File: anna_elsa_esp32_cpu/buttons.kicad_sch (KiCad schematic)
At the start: 26 parts, among them J14 DOOR_SW, J22 BTN_SWITCHES, J23 BTN_LAMPS, Q3 ULN2803ADWR, U8 MCP23017-E_SO

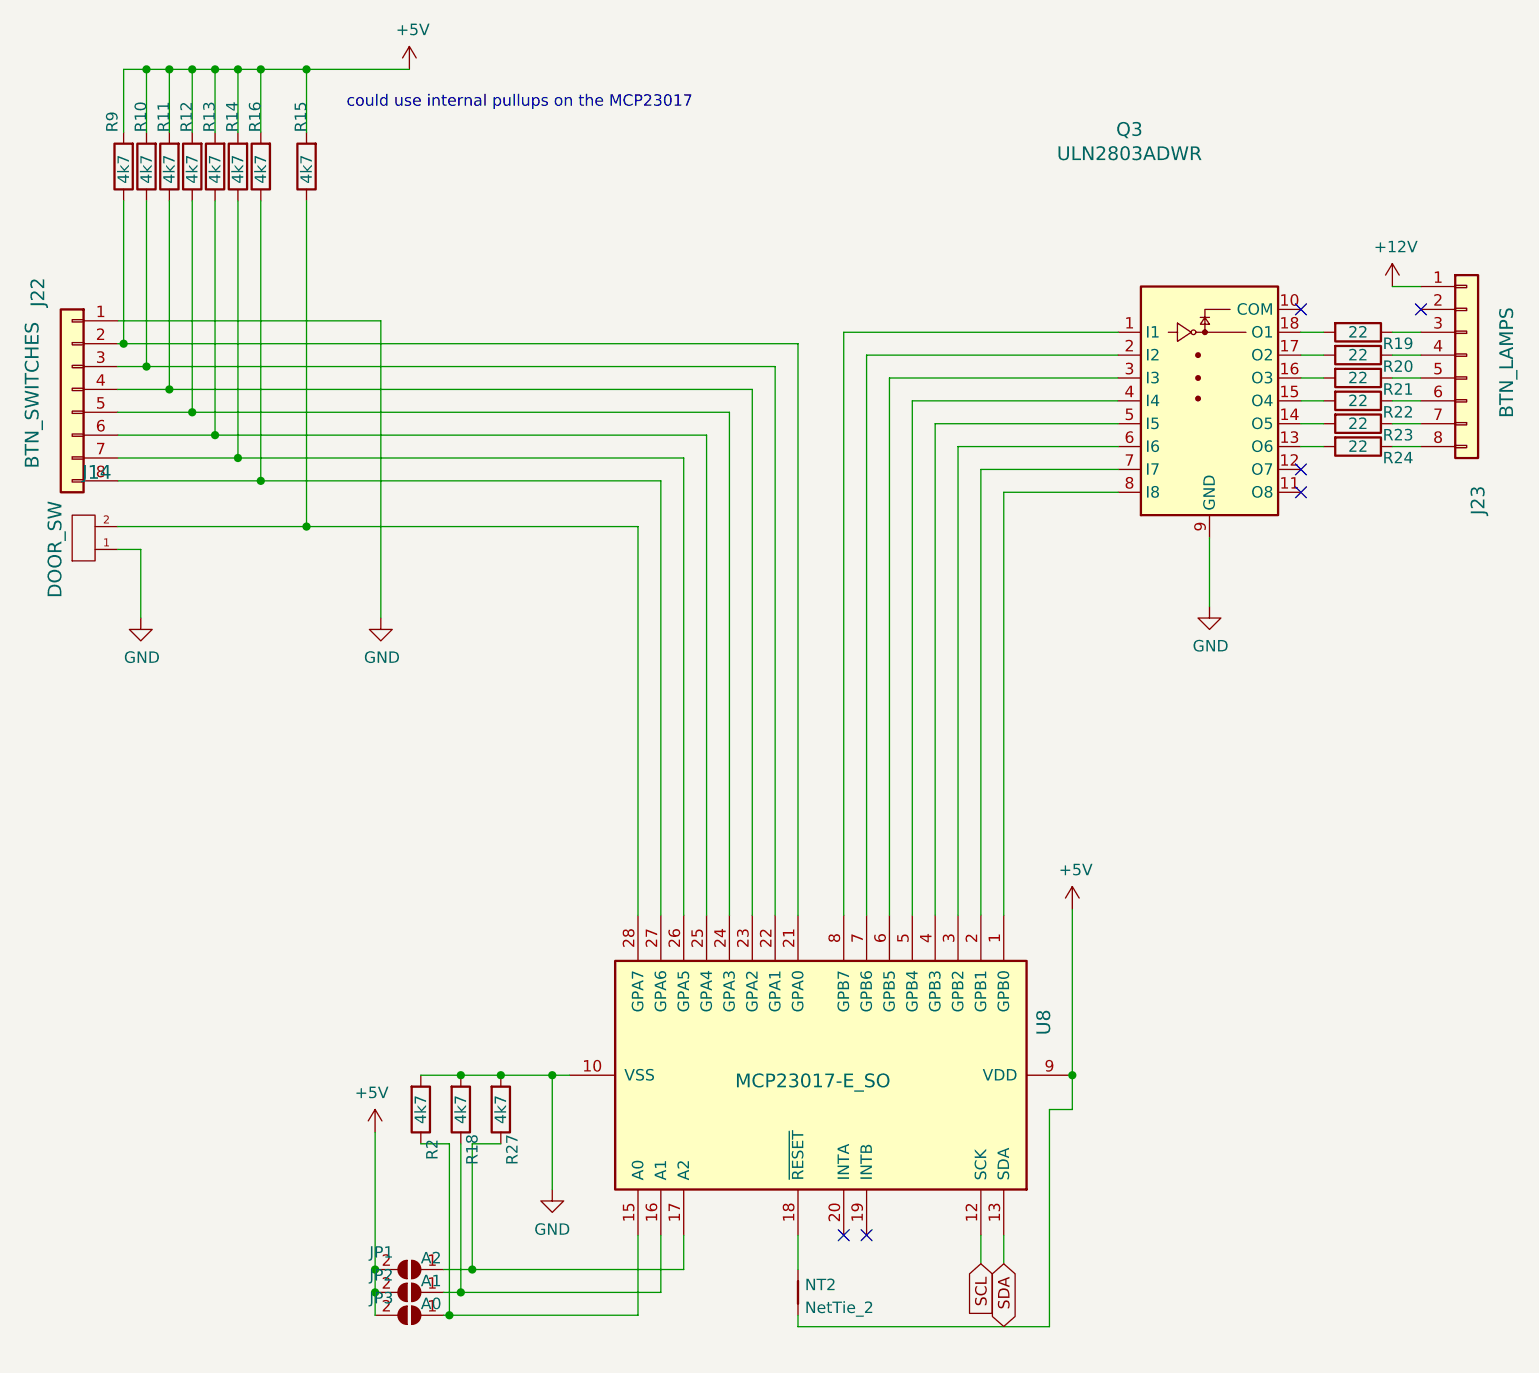
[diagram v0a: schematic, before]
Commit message: Added current cpu pcb and removed old
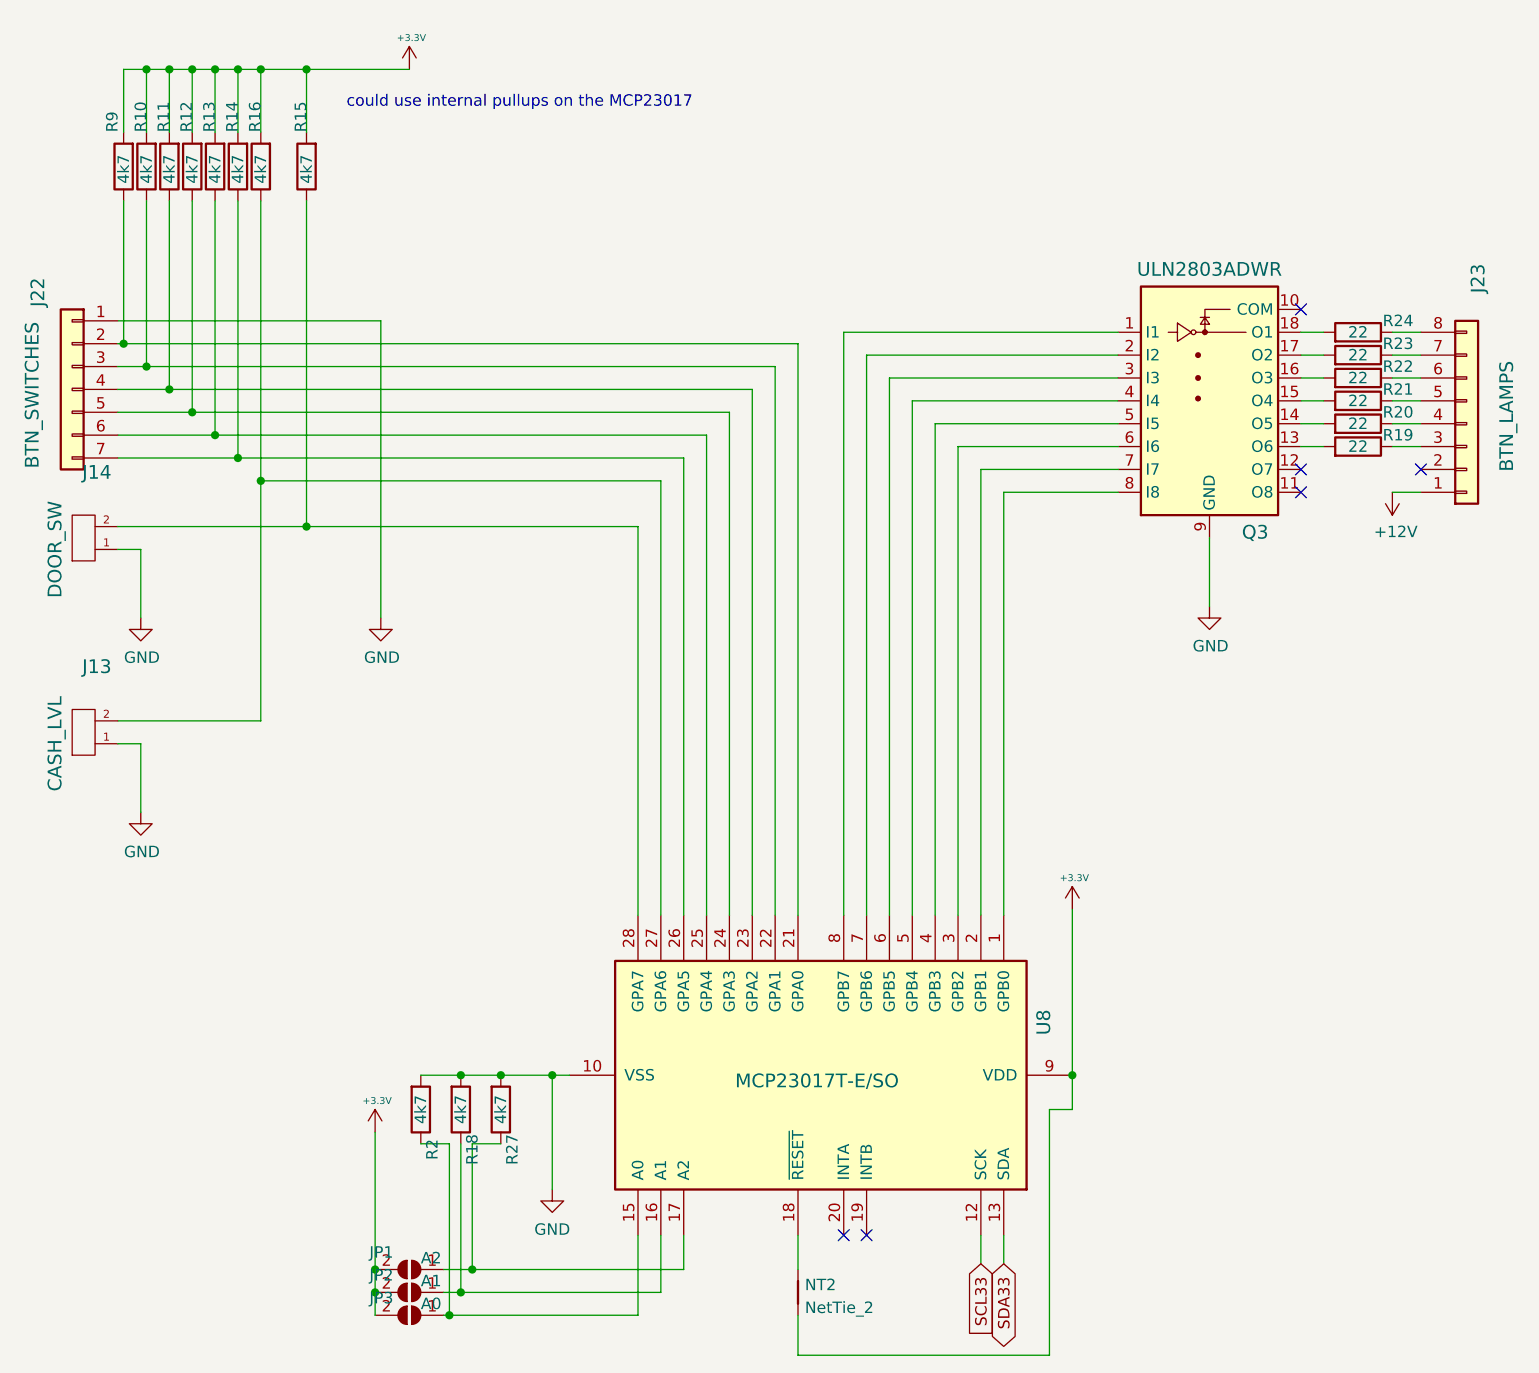
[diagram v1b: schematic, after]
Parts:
- added J13: CASH_LVL, Connector_JST:JST_XH_B2B-XH-A_1x02_P2.50mm_Vertical, symbol w_connectors:HEADER_2
- J22: footprint Connector_JST:JST_XH_B8B-XH-A_1x08_P2.50mm_Vertical -> Connector_JST:JST_XH_B7B-XH-A_1x07_P2.50mm_Vertical; symbol Connector_Generic:Conn_01x08 -> Connector_Generic:Conn_01x07
- U8: value MCP23017-E_SO -> MCP23017T-E/SO; JLC SOIC-28_300mil -> C629440; LCSC C47023 -> C629440
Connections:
- net GND: now also J13.1
- net at Q3.13 (O6): now also R19.2; no longer R24.2
- net at Q3.14 (O5): now also R20.2; no longer R23.2
- net at Q3.15 (O4): now also R21.2; no longer R22.2
- net at Q3.16 (O3): now also R22.2; no longer R21.2
- net at Q3.17 (O2): now also R23.2; no longer R20.2
- net at Q3.18 (O1): now also R24.2; no longer R19.2
- net at R16.1, U8.27 (GPA6): now also J13.2; no longer J22.8 (Pin_8)
- net +5V renamed +3.3V
- net SCL renamed SCL33
- net SDA renamed SDA33
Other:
- moved on the sheet: J23, R19, R20, R21, R22, R23, R24
